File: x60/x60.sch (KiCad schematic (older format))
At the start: 150 parts, among them SW1 SW_Push, U1 ATmega32U4-AU, Y1 16mhz

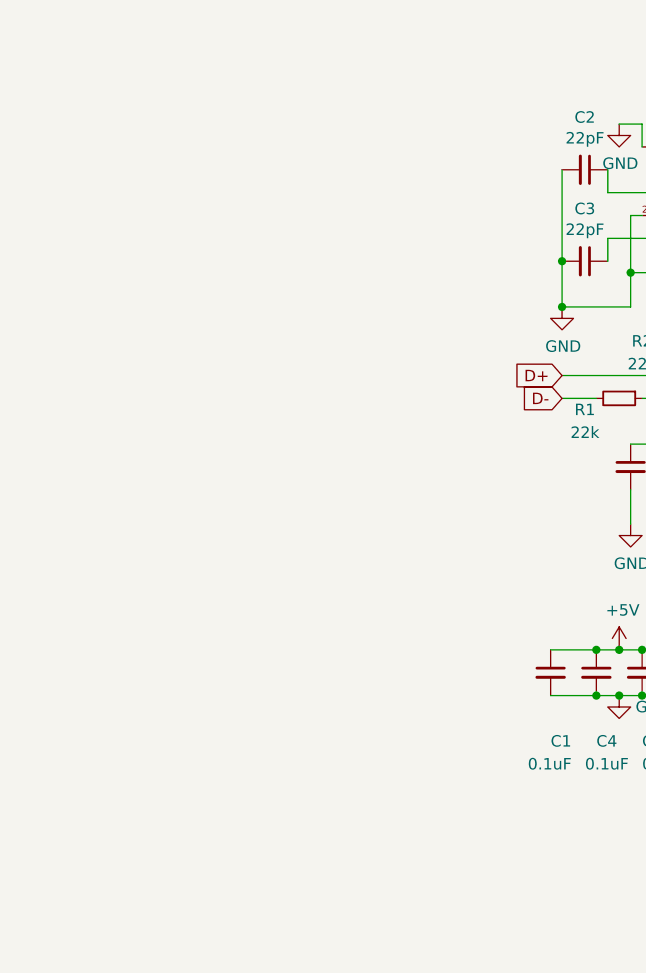
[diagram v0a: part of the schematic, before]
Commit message: added usb c to schematic
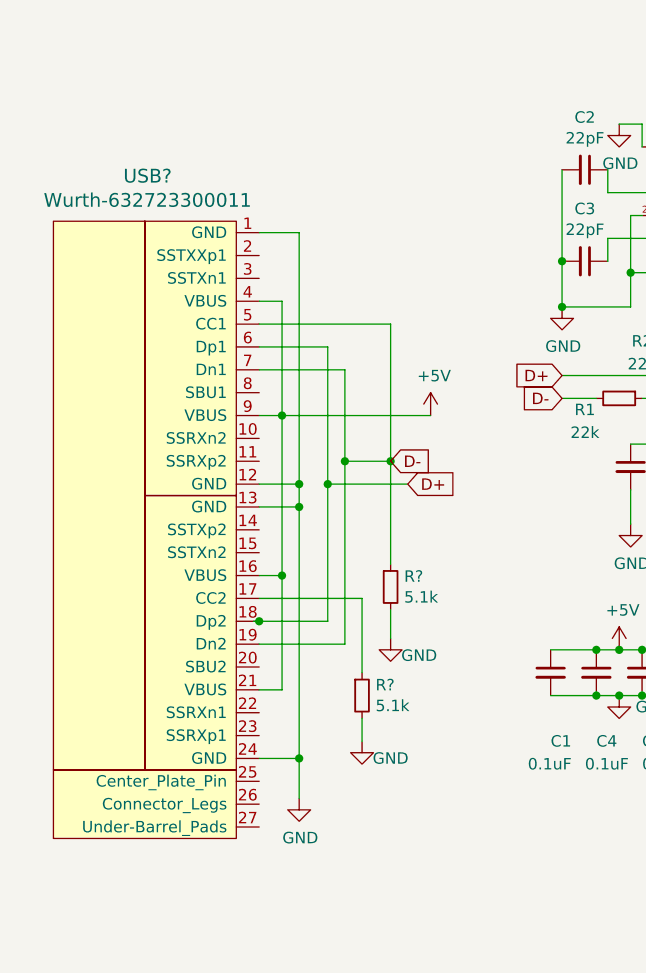
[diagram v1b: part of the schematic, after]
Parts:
- added R? (x2): 5.1k, symbol Device:R_Small
- added USB?: Wurth-632723300011, symbol Type-C:Wurth-632723300011
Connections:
- net +5V: now also USB?.16 (VBUS), USB?.21 (VBUS), USB?.4 (VBUS), USB?.9 (VBUS)
- net D+: now also USB?.18 (Dp2), USB?.6 (Dp1)
- net D-: now also R?.1, USB?.19 (Dn2), USB?.5 (CC1), USB?.7 (Dn1)
- net GND: now also R?.2, R?.2, USB?.1 (GND), USB?.12 (GND), USB?.13 (GND), USB?.24 (GND)
- new net: R?.1, USB?.17 (CC2)
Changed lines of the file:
@@
 Text GLabel 6075 6275 2    50   Input ~ 0
 COL14
+$Comp
+L Type-C:Wurth-632723300011 USB?
+U 1 1 61808720
+P 2600 6800
+F 0 "USB?" H 2212 8197 60  0000 C CNN
+F 1 "Wurth-632723300011" H 2212 8091 60  0000 C CNN
+F 2 "" H 2600 6800 60  0001 C CNN
+F 3 "" H 2600 6800 60  0001 C CNN
+	1    2600 6800
+	1    0    0    -1
+$EndComp
+Wire Wire Line
+	2675 7350 2700 7350
+Wire Wire Line
+	3000 7350 3000 6750
+Wire Wire Line
+	3000 6150 2700 6150
+Connection ~ 2700 7350
+Wire Wire Line
+	2700 7350 3000 7350
+Wire Wire Line
+	2700 6250 3075 6250
+Wire Wire Line
+	3075 6250 3075 6650
+Wire Wire Line
+	3075 7450 2700 7450
+Wire Wire Line
+	3000 6750 3350 6750
+Connection ~ 3000 6750
+Wire Wire Line
+	3000 6750 3000 6150
+Text GLabel 3350 6750 2    50   Input ~ 0
+D+
+Wire Wire Line
+	3075 6650 3275 6650
+Connection ~ 3075 6650
+Wire Wire Line
+	3075 6650 3075 7450
+Text GLabel 3275 6650 2    50   Input ~ 0
+D-
+Wire Wire Line
+	2700 7950 2875 7950
+Wire Wire Line
+	2875 6850 2700 6850
+Wire Wire Line
+	2700 6750 2875 6750
+Wire Wire Line
+	2875 6750 2875 6850
+Connection ~ 2875 6850
+Wire Wire Line
+	2875 6750 2875 5650
+Wire Wire Line
+	2875 5650 2700 5650
+Connection ~ 2875 6750
+$Comp
+L power:GND #PWR?
+U 1 1 6198D4D5
+P 2875 8125
+F 0 "#PWR?" H 2875 7875 50  0001 C CNN
+F 1 "GND" H 2880 7952 50  0000 C CNN
+F 2 "" H 2875 8125 50  0001 C CNN
+F 3 "" H 2875 8125 50  0001 C CNN
+	1    2875 8125
+	1    0    0    -1
+$EndComp
+Wire Wire Line
+	2700 7650 2800 7650
+Wire Wire Line
+	2800 7650 2800 7150
+Wire Wire Line
+	2800 7150 2700 7150
+Wire Wire Line
+	2800 7150 2800 6450
+Wire Wire Line
+	2800 6450 2700 6450
+Connection ~ 2800 7150
+Wire Wire Line
+	2800 6450 2800 5950
+Wire Wire Line
+	2800 5950 2700 5950
+Connection ~ 2800 6450
+Wire Wire Line
+	2700 6050 3275 6050
+Wire Wire Line
+	3275 6050 3275 6650
+Connection ~ 3275 6650
+Wire Wire Line
+	3275 6650 3275 7100
+$Comp
+L Device:R_Small R?
+U 1 1 61A38DF8
+P 3275 7200
+F 0 "R?" H 3334 7246 50  0000 L CNN
+F 1 "5.1k" H 3334 7155 50  0000 L CNN
+F 2 "" H 3275 7200 50  0001 C CNN
+F 3 "~" H 3275 7200 50  0001 C CNN
+	1    3275 7200
+	1    0    0    -1
+$EndComp
+$Comp
+L power:GND #PWR?
+U 1 1 61A39C9A
+P 3275 7425
+F 0 "#PWR?" H 3275 7175 50  0001 C CNN
+F 1 "GND" H 3400 7350 50  0000 C CNN
+F 2 "" H 3275 7425 50  0001 C CNN
+F 3 "" H 3275 7425 50  0001 C CNN
+	1    3275 7425
+	1    0    0    -1
+$EndComp
+Wire Wire Line
+	3275 7300 3275 7425
+Wire Wire Line
+	2700 7250 3150 7250
+Wire Wire Line
+	3150 7250 3150 7575
+$Comp
+L Device:R_Small R?
+U 1 1 61A910AE
+P 3150 7675
+F 0 "R?" H 3209 7721 50  0000 L CNN
+F 1 "5.1k" H 3209 7630 50  0000 L CNN
+F 2 "" H 3150 7675 50  0001 C CNN
+F 3 "~" H 3150 7675 50  0001 C CNN
+	1    3150 7675
+	1    0    0    -1
+$EndComp
+Wire Wire Line
+	2875 6850 2875 7950
+Wire Wire Line
+	2875 7950 2875 8125
+Connection ~ 2875 7950
+$Comp
+L power:GND #PWR?
+U 1 1 61ABD2BB
+P 3150 7875
+F 0 "#PWR?" H 3150 7625 50  0001 C CNN
+F 1 "GND" H 3275 7800 50  0000 C CNN
+F 2 "" H 3150 7875 50  0001 C CNN
+F 3 "" H 3150 7875 50  0001 C CNN
+	1    3150 7875
+	1    0    0    -1
+$EndComp
+Wire Wire Line
+	3150 7775 3150 7875
+Wire Wire Line
+	2800 6450 3450 6450
+$Comp
+L power:+5V #PWR?
+U 1 1 61B14B63
+P 3450 6450
+F 0 "#PWR?" H 3450 6300 50  0001 C CNN
+F 1 "+5V" H 3465 6623 50  0000 C CNN
+F 2 "" H 3450 6450 50  0001 C CNN
+F 3 "" H 3450 6450 50  0001 C CNN
+	1    3450 6450
+	1    0    0    -1
+$EndComp
 $EndSCHEMATC

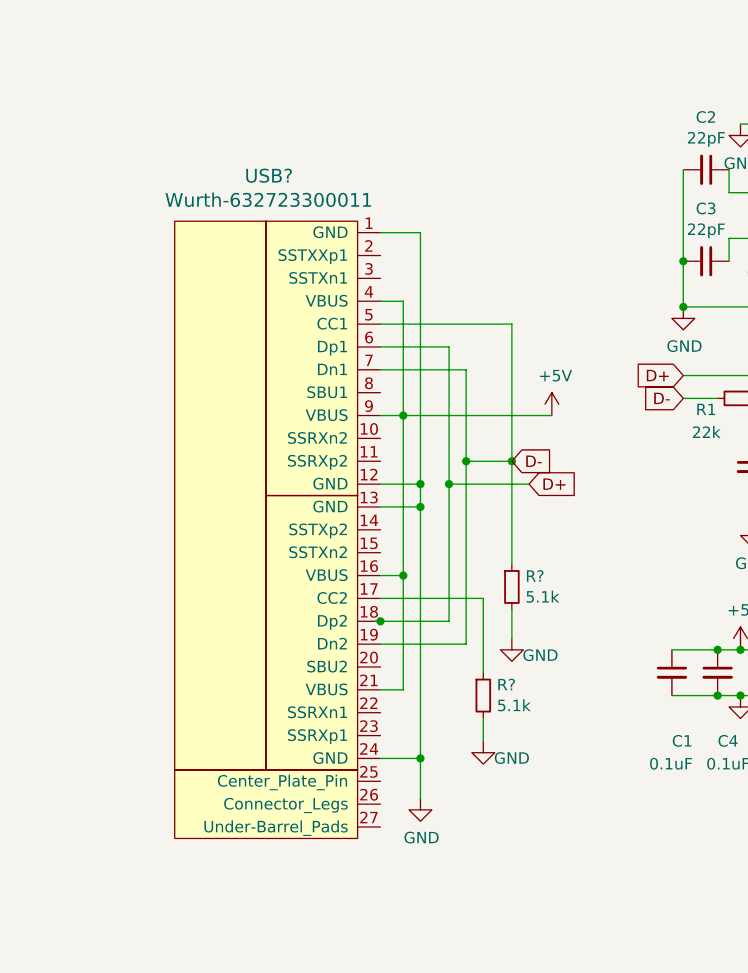
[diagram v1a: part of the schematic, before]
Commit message: updated schematic for usb
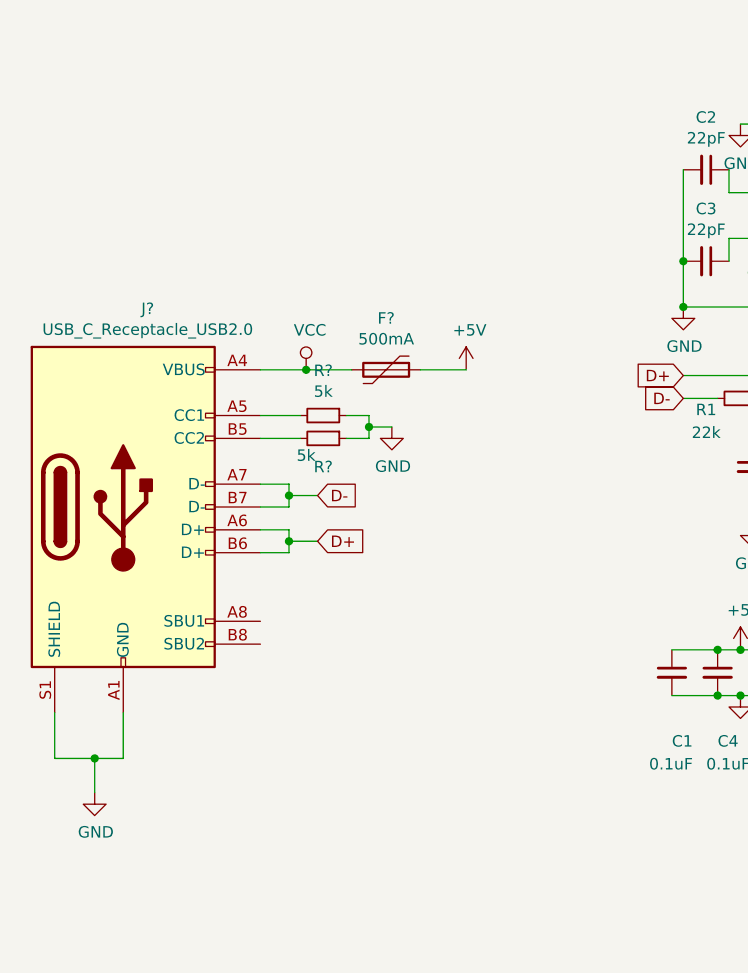
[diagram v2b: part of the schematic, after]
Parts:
- removed R? (x2): 5.1k, symbol Device:R_Small
- removed USB?: Wurth-632723300011, symbol Type-C:Wurth-632723300011
- added F?: 500mA, symbol Device:Polyfuse
- added J?: USB_C_Receptacle_USB2.0, symbol Connector:USB_C_Receptacle_USB2.0
- added R? (x2): 5k, symbol Device:R_Small
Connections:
- net +5V: now also F?.1
- net D+: now also J?.A6 (D+), J?.B6 (D+)
- net D-: now also J?.A7 (D-), J?.B7 (D-)
- net GND: now also J?.A1 (GND), J?.A12 (GND), J?.B1 (GND), J?.B12 (GND), J?.S1 (SHIELD), R?.1, R?.1
- new net: J?.A5 (CC1), R?.2
- new net: J?.B5 (CC2), R?.2
- new net VCC: F?.2, J?.A4 (VBUS), J?.A9 (VBUS), J?.B4 (VBUS), J?.B9 (VBUS)
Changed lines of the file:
@@
 COL14
 $Comp
-L Type-C:Wurth-632723300011 USB?
-U 1 1 61808720
-P 2600 6800
-F 0 "USB?" H 2212 8197 60  0000 C CNN
-F 1 "Wurth-632723300011" H 2212 8091 60  0000 C CNN
-F 2 "" H 2600 6800 60  0001 C CNN
-F 3 "" H 2600 6800 60  0001 C CNN
-	1    2600 6800
+L Connector:USB_C_Receptacle_USB2.0 J?
+U 1 1 61856F2E
+P 1575 6850
+F 0 "J?" H 1682 7717 50  0000 C CNN
+F 1 "USB_C_Receptacle_USB2.0" H 1682 7626 50  0000 C CNN
+F 2 "" H 1725 6850 50  0001 C CNN
+F 3 "https://www.usb.org/sites/default/files/documents/usb_type-c.zip" H 1725 6850 50  0001 C CNN
+	1    1575 6850
 	1    0    0    -1
 $EndComp
 Wire Wire Line
-	2675 7350 2700 7350
+	1275 7750 1275 7950
 Wire Wire Line
-	3000 7350 3000 6750
+	1275 7950 1450 7950
 Wire Wire Line
-	3000 6150 2700 6150
-Connection ~ 2700 7350
+	1575 7950 1575 7750
 Wire Wire Line
-	2700 7350 3000 7350
+	1450 7950 1450 8100
+Connection ~ 1450 7950
 Wire Wire Line
-	2700 6250 3075 6250
-Wire Wire Line
-	3075 6250 3075 6650
-Wire Wire Line
-	3075 7450 2700 7450
-Wire Wire Line
-	3000 6750 3350 6750
-Connection ~ 3000 6750
-Wire Wire Line
-	3000 6750 3000 6150
-Text GLabel 3350 6750 2    50   Input ~ 0
-D+
-Wire Wire Line
-	3075 6650 3275 6650
-Connection ~ 3075 6650
-Wire Wire Line
-	3075 6650 3075 7450
-Text GLabel 3275 6650 2    50   Input ~ 0
-D-
-Wire Wire Line
-	2700 7950 2875 7950
-Wire Wire Line
-	2875 6850 2700 6850
-Wire Wire Line
-	2700 6750 2875 6750
-Wire Wire Line
-	2875 6750 2875 6850
-Connection ~ 2875 6850
-Wire Wire Line
-	2875 6750 2875 5650
-Wire Wire Line
-	2875 5650 2700 5650
-Connection ~ 2875 6750
+	1450 7950 1575 7950
 $Comp
 L power:GND #PWR?
-U 1 1 6198D4D5
-P 2875 8125
-F 0 "#PWR?" H 2875 7875 50  0001 C CNN
-F 1 "GND" H 2880 7952 50  0000 C CNN
-F 2 "" H 2875 8125 50  0001 C CNN
-F 3 "" H 2875 8125 50  0001 C CNN
-	1    2875 8125
+U 1 1 618A0C63
+P 1450 8100
+F 0 "#PWR?" H 1450 7850 50  0001 C CNN
+F 1 "GND" H 1455 7927 50  0000 C CNN
+F 2 "" H 1450 8100 50  0001 C CNN
+F 3 "" H 1450 8100 50  0001 C CNN
+	1    1450 8100
 	1    0    0    -1
 $EndComp
 Wire Wire Line
-	2700 7650 2800 7650
+	2175 6950 2300 6950
 Wire Wire Line
-	2800 7650 2800 7150
+	2300 6950 2300 7000
 Wire Wire Line
-	2800 7150 2700 7150
+	2300 7050 2175 7050
 Wire Wire Line
-	2800 7150 2800 6450
+	2300 7000 2425 7000
+Connection ~ 2300 7000
 Wire Wire Line
-	2800 6450 2700 6450
-Connection ~ 2800 7150
+	2300 7000 2300 7050
+Text GLabel 2425 7000 2    50   Input ~ 0
+D+
 Wire Wire Line
-	2800 6450 2800 5950
+	2175 6750 2300 6750
 Wire Wire Line
-	2800 5950 2700 5950
-Connection ~ 2800 6450
+	2300 6750 2300 6800
 Wire Wire Line
-	2700 6050 3275 6050
+	2300 6850 2175 6850
 Wire Wire Line
-	3275 6050 3275 6650
-Connection ~ 3275 6650
+	2300 6800 2425 6800
+Connection ~ 2300 6800
 Wire Wire Line
-	3275 6650 3275 7100
+	2300 6800 2300 6850
+Text GLabel 2425 6800 2    50   Input ~ 0
+D-
+Wire Wire Line
+	2175 6450 2350 6450
+Wire Wire Line
+	2175 6550 2350 6550
 $Comp
 L Device:R_Small R?
-U 1 1 61A38DF8
-P 3275 7200
-F 0 "R?" H 3334 7246 50  0000 L CNN
-F 1 "5.1k" H 3334 7155 50  0000 L CNN
-F 2 "" H 3275 7200 50  0001 C CNN
-F 3 "~" H 3275 7200 50  0001 C CNN
-	1    3275 7200
-	1    0    0    -1
+U 1 1 6198B265
+P 2450 6450
+F 0 "R?" V 2254 6450 50  0000 C CNN
+F 1 "5k" V 2345 6450 50  0000 C CNN
+F 2 "" H 2450 6450 50  0001 C CNN
+F 3 "~" H 2450 6450 50  0001 C CNN
+	1    2450 6450
+	0    1    1    0
 $EndComp
 $Comp
+L Device:R_Small R?
+U 1 1 6198B998
+P 2450 6550
+F 0 "R?" V 2575 6550 50  0000 C CNN
+F 1 "5k" V 2525 6475 50  0000 C CNN
+F 2 "" H 2450 6550 50  0001 C CNN
+F 3 "~" H 2450 6550 50  0001 C CNN
+	1    2450 6550
+	0    1    1    0
+$EndComp
+Wire Wire Line
+	2550 6550 2650 6550
+Wire Wire Line
+	2650 6550 2650 6500
+Wire Wire Line
+	2650 6450 2550 6450
+Wire Wire Line
+	2650 6500 2750 6500
+Connection ~ 2650 6500
+Wire Wire Line
+	2650 6500 2650 6450
+$Comp
 L power:GND #PWR?
-U 1 1 61A39C9A
-P 3275 7425
-F 0 "#PWR?" H 3275 7175 50  0001 C CNN
-F 1 "GND" H 3400 7350 50  0000 C CNN
-F 2 "" H 3275 7425 50  0001 C CNN
-F 3 "" H 3275 7425 50  0001 C CNN
-	1    3275 7425
+U 1 1 61A598C2
+P 2750 6500
+F 0 "#PWR?" H 2750 6250 50  0001 C CNN
+F 1 "GND" H 2755 6327 50  0000 C CNN
+F 2 "" H 2750 6500 50  0001 C CNN
+F 3 "" H 2750 6500 50  0001 C CNN
+	1    2750 6500
 	1    0    0    -1
 $EndComp
 Wire Wire Line
-	3275 7300 3275 7425
-Wire Wire Line
-	2700 7250 3150 7250
-Wire Wire Line
-	3150 7250 3150 7575
+	2175 6250 2375 6250
 $Comp
-L Device:R_Small R?
-U 1 1 61A910AE
-P 3150 7675
-F 0 "R?" H 3209 7721 50  0000 L CNN
-F 1 "5.1k" H 3209 7630 50  0000 L CNN
-F 2 "" H 3150 7675 50  0001 C CNN
-F 3 "~" H 3150 7675 50  0001 C CNN
-	1    3150 7675
+L power:VCC #PWR?
+U 1 1 61A8443F
+P 2375 6250
+F 0 "#PWR?" H 2375 6100 50  0001 C CNN
+F 1 "VCC" H 2392 6423 50  0000 C CNN
+F 2 "" H 2375 6250 50  0001 C CNN
+F 3 "" H 2375 6250 50  0001 C CNN
+	1    2375 6250
 	1    0    0    -1
 $EndComp
 Wire Wire Line
-	2875 6850 2875 7950
+	2375 6250 2575 6250
+Connection ~ 2375 6250
+$Comp
+L Device:Polyfuse F?
+U 1 1 61AAEE5C
+P 2725 6250
+F 0 "F?" V 2500 6250 50  0000 C CNN
+F 1 "500mA" V 2591 6250 50  0000 C CNN
+F 2 "" H 2775 6050 50  0001 L CNN
+F 3 "~" H 2725 6250 50  0001 C CNN
+	1    2725 6250
+	0    1    1    0
+$EndComp
 Wire Wire Line
-	2875 7950 2875 8125
-Connection ~ 2875 7950
+	2875 6250 3075 6250
 $Comp
-L power:GND #PWR?
-U 1 1 61ABD2BB
-P 3150 7875
-F 0 "#PWR?" H 3150 7625 50  0001 C CNN
-F 1 "GND" H 3275 7800 50  0000 C CNN
-F 2 "" H 3150 7875 50  0001 C CNN
-F 3 "" H 3150 7875 50  0001 C CNN
-	1    3150 7875
+L power:+5V #PWR?
+U 1 1 61ADB3C8
+P 3075 6250
+F 0 "#PWR?" H 3075 6100 50  0001 C CNN
+F 1 "+5V" H 3090 6423 50  0000 C CNN
+F 2 "" H 3075 6250 50  0001 C CNN
+F 3 "" H 3075 6250 50  0001 C CNN
+	1    3075 6250
 	1    0    0    -1
 $EndComp
-Wire Wire Line
-	3150 7775 3150 7875
-Wire Wire Line
-	2800 6450 3450 6450
-$Comp
-L power:+5V #PWR?
-U 1 1 61B14B63
-P 3450 6450
-F 0 "#PWR?" H 3450 6300 50  0001 C CNN
-F 1 "+5V" H 3465 6623 50  0000 C CNN
-F 2 "" H 3450 6450 50  0001 C CNN
-F 3 "" H 3450 6450 50  0001 C CNN
-	1    3450 6450
-	1    0    0    -1
-$EndComp
